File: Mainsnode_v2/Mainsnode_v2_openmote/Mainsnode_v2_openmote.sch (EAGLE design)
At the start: 72 parts, among them IC1 7805T, J2 WIRE_HOLE-14AWG, J3 WIRE_HOLE-14AWG, J4 HOLE, J5 HOLE, J6 HOLE, J7 HOLE, K1 S216S01F, Q1 STGD5NB120SZT4, Q2 3.579545MHz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

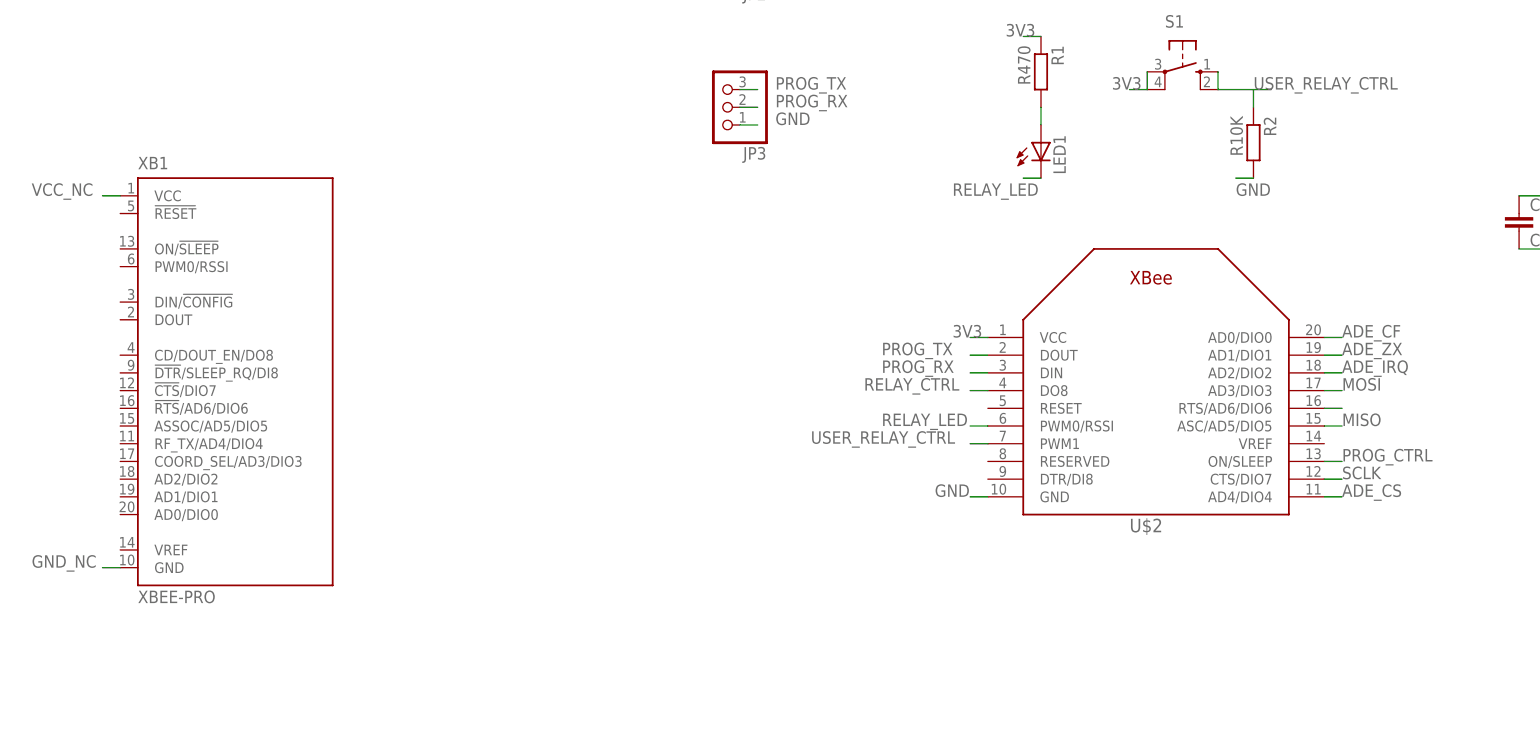
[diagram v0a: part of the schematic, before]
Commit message: Finish PCB Mainsnode_V2_openmote
Ferrite bead DigiKey 240-2418 and 240-2520 and casing have not been
ordered yet.
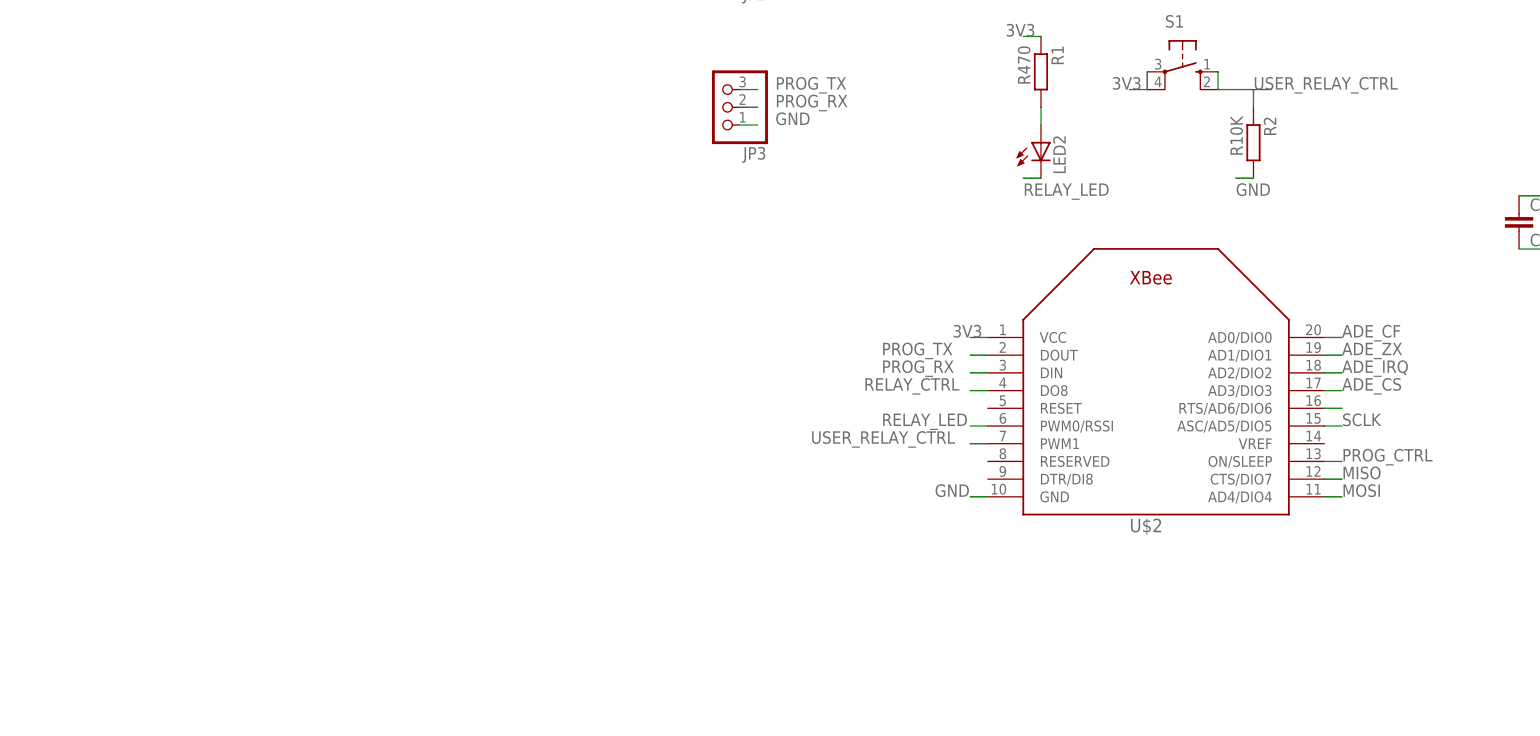
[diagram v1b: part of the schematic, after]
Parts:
- removed LED1: (no value), adafruit:LEDCHIP-LED0805
- removed XB1: XBEE-PRO, maxstream:XBEE-PRO
- added LED2: (no value), adafruit:LED3MM
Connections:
- removed net GND_NC: XB1.GND
- removed net VCC_NC: XB1.VCC
- net ADE_CS: now also U$2.AD3/DIO3; no longer U$2.AD4/DIO4
- net MISO: now also U$2.CTS/DIO7; no longer U$2.ASC/AD5/DIO5
- net MOSI: now also U$2.AD4/DIO4; no longer U$2.AD3/DIO3
- net N$2: now also LED2.A; no longer LED1.A
- net RELAY_LED: now also LED2.C; no longer LED1.C
- net SCLK: now also U$2.ASC/AD5/DIO5; no longer U$2.CTS/DIO7
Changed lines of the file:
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@@
 <parts>
 <part name="R1" library="resistor" deviceset="R-EU_" device="R0805" value="R470"/>
-<part name="LED1" library="adafruit" deviceset="LED" device="CHIP-LED0805"/>
 <part name="R2" library="resistor" deviceset="R-EU_" device="R0805" value="R10K"/>
 <part name="S1" library="switch-omron" deviceset="10-XX" device=""/>
@@
 <part name="JP2" library="pinhead" deviceset="PINHD-1X2" device=""/>
 <part name="JP3" library="pinhead" deviceset="PINHD-1X3" device=""/>
-<part name="XB1" library="maxstream" deviceset="XBEE" device="-PRO"/>
 <part name="D4" library="semicon-smd-ipc" deviceset="D-" device="SOD-80" value="1N4148"/>
 <part name="L5" library="resistor" deviceset="L-EU" device="L3216C" value="BLM31PG330SN1"/>
+<part name="LED2" library="adafruit" deviceset="LED" device="3MM"/>
 </parts>
 <sheets>
@@
 <instances>
 <instance part="R1" gate="G$1" x="106.68" y="109.22" rot="R270"/>
-<instance part="LED1" gate="G$1" x="106.68" y="99.06"/>
 <instance part="R2" gate="G$1" x="137.16" y="99.06" rot="R270"/>
 <instance part="S1" gate="1" x="127" y="109.22" rot="R270"/>
@@
 <instance part="JP2" gate="G$1" x="60.96" y="127" rot="R180"/>
 <instance part="JP3" gate="A" x="60.96" y="104.14" rot="R180"/>
-<instance part="XB1" gate="G$1" x="-10.16" y="66.04"/>
 <instance part="D4" gate="G$1" x="-15.24" y="-93.98" rot="R90"/>
 <instance part="L5" gate="G$1" x="175.26" y="-55.88" rot="R90"/>
+<instance part="LED2" gate="G$1" x="106.68" y="99.06"/>
 </instances>
 <busses>
@@
 </segment>
 </net>
-<net name="N$2" class="0">
-<segment>
-<pinref part="R1" gate="G$1" pin="2"/>
-<pinref part="LED1" gate="G$1" pin="A"/>
-<wire x1="106.68" y1="104.14" x2="106.68" y2="101.6" width="0.1524" layer="91"/>
-</segment>
-</net>
 <net name="RELAY_LED" class="0">
-<segment>
-<pinref part="LED1" gate="G$1" pin="C"/>
-<wire x1="106.68" y1="93.98" x2="104.14" y2="93.98" width="0.1524" layer="91"/>
-<label x="93.98" y="91.44" size="1.778" layer="95"/>
-</segment>
 <segment>
 <pinref part="U$2" gate="G$1" pin="PWM0/RSSI"/>
 <wire x1="99.06" y1="58.42" x2="96.52" y2="58.42" width="0.1524" layer="91"/>
 <label x="83.82" y="58.42" size="1.778" layer="95"/>
+</segment>
+<segment>
+<pinref part="LED2" gate="G$1" pin="C"/>
+<wire x1="106.68" y1="93.98" x2="104.14" y2="93.98" width="0.1524" layer="91"/>
+<label x="104.14" y="91.44" size="1.778" layer="95"/>
 </segment>
 </net>
@@
 </segment>
 <segment>
-<pinref part="U$2" gate="G$1" pin="AD4/DIO4"/>
-<wire x1="147.32" y1="48.26" x2="149.86" y2="48.26" width="0.1524" layer="91"/>
-<label x="149.86" y="48.26" size="1.778" layer="95"/>
+<pinref part="U$2" gate="G$1" pin="AD3/DIO3"/>
+<wire x1="147.32" y1="63.5" x2="149.86" y2="63.5" width="0.1524" layer="91"/>
+<label x="149.86" y="63.5" size="1.778" layer="95"/>
 </segment>
 </net>
@@
 </segment>
 <segment>
-<pinref part="U$2" gate="G$1" pin="ASC/AD5/DIO5"/>
-<wire x1="147.32" y1="58.42" x2="149.86" y2="58.42" width="0.1524" layer="91"/>
-<label x="149.86" y="58.42" size="1.778" layer="95"/>
+<pinref part="U$2" gate="G$1" pin="CTS/DIO7"/>
+<wire x1="147.32" y1="50.8" x2="149.86" y2="50.8" width="0.1524" layer="91"/>
+<label x="149.86" y="50.8" size="1.778" layer="95"/>
 </segment>
 </net>
@@
 </segment>
 <segment>
-<pinref part="U$2" gate="G$1" pin="AD3/DIO3"/>
-<wire x1="147.32" y1="63.5" x2="149.86" y2="63.5" width="0.1524" layer="91"/>
-<label x="149.86" y="63.5" size="1.778" layer="95"/>
+<pinref part="U$2" gate="G$1" pin="AD4/DIO4"/>
+<wire x1="147.32" y1="48.26" x2="149.86" y2="48.26" width="0.1524" layer="91"/>
+<label x="149.86" y="48.26" size="1.778" layer="95"/>
 </segment>
 </net>
@@
 </segment>
 <segment>
-<pinref part="U$2" gate="G$1" pin="CTS/DIO7"/>
-<wire x1="147.32" y1="50.8" x2="149.86" y2="50.8" width="0.1524" layer="91"/>
-<label x="149.86" y="50.8" size="1.778" layer="95"/>
+<pinref part="U$2" gate="G$1" pin="ASC/AD5/DIO5"/>
+<wire x1="147.32" y1="58.42" x2="149.86" y2="58.42" width="0.1524" layer="91"/>
+<label x="149.86" y="58.42" size="1.778" layer="95"/>
 </segment>
 </net>
@@
 </segment>
 </net>
-<net name="VCC_NC" class="0">
-<segment>
-<pinref part="XB1" gate="G$1" pin="VCC"/>
-<wire x1="-25.4" y1="91.44" x2="-27.94" y2="91.44" width="0.1524" layer="91"/>
-<label x="-38.1" y="91.44" size="1.778" layer="95"/>
-</segment>
-</net>
-<net name="GND_NC" class="0">
-<segment>
-<pinref part="XB1" gate="G$1" pin="GND"/>
-<wire x1="-25.4" y1="38.1" x2="-27.94" y2="38.1" width="0.1524" layer="91"/>
-<label x="-38.1" y="38.1" size="1.778" layer="95"/>
-</segment>
-</net>
 <net name="N$1" class="0">
 <segment>
@@
 </segment>
 </net>
+<net name="N$2" class="0">
+<segment>
+<pinref part="R1" gate="G$1" pin="2"/>
+<pinref part="LED2" gate="G$1" pin="A"/>
+<wire x1="106.68" y1="104.14" x2="106.68" y2="101.6" width="0.1524" layer="91"/>
+</segment>
+</net>
